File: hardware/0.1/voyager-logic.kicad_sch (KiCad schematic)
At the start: 3 parts, among them J1 USB_C_Receptacle, U1 HD3SS3220, U2 CYUSB3014-BZXx

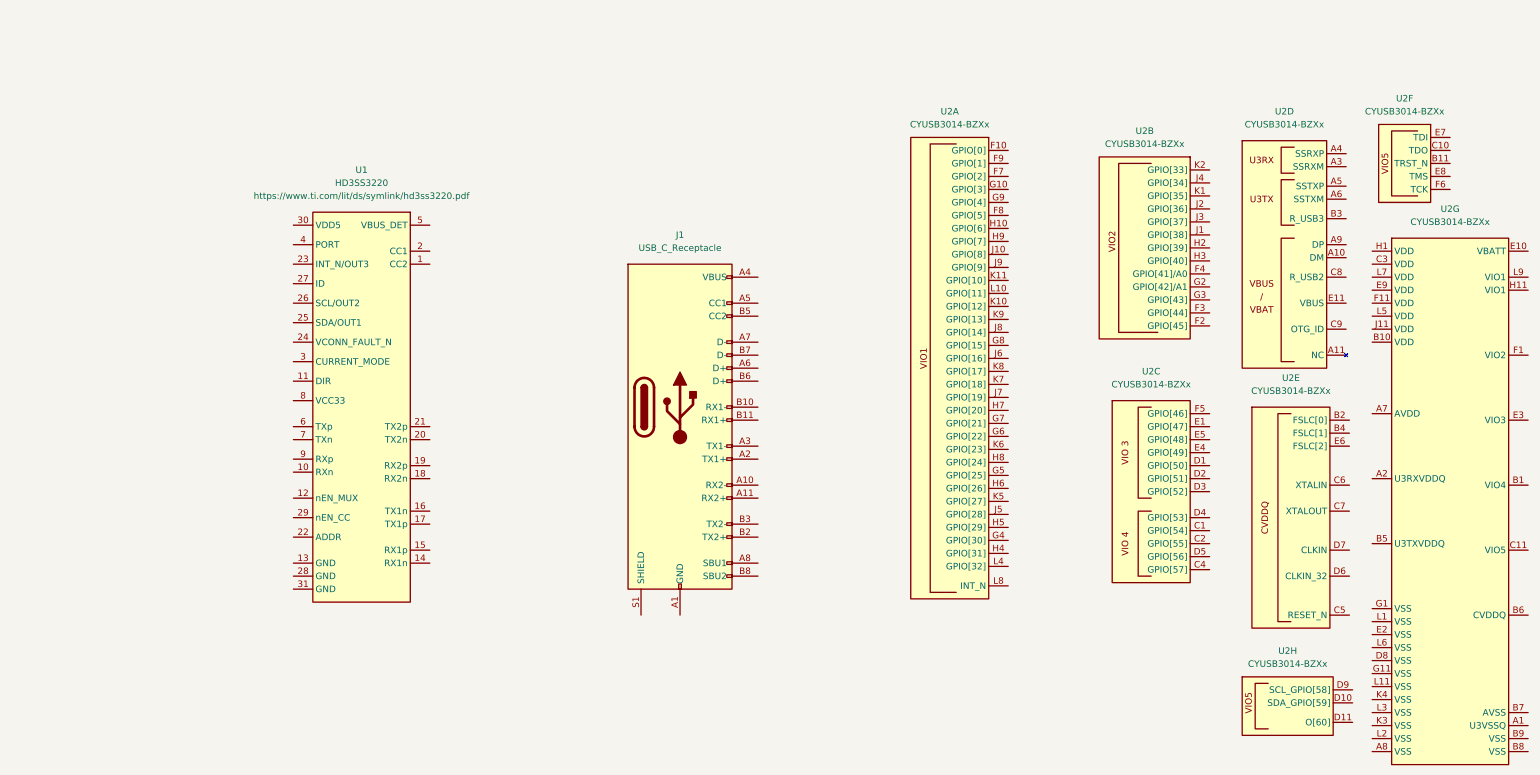
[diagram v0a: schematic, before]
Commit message: wip usb c design
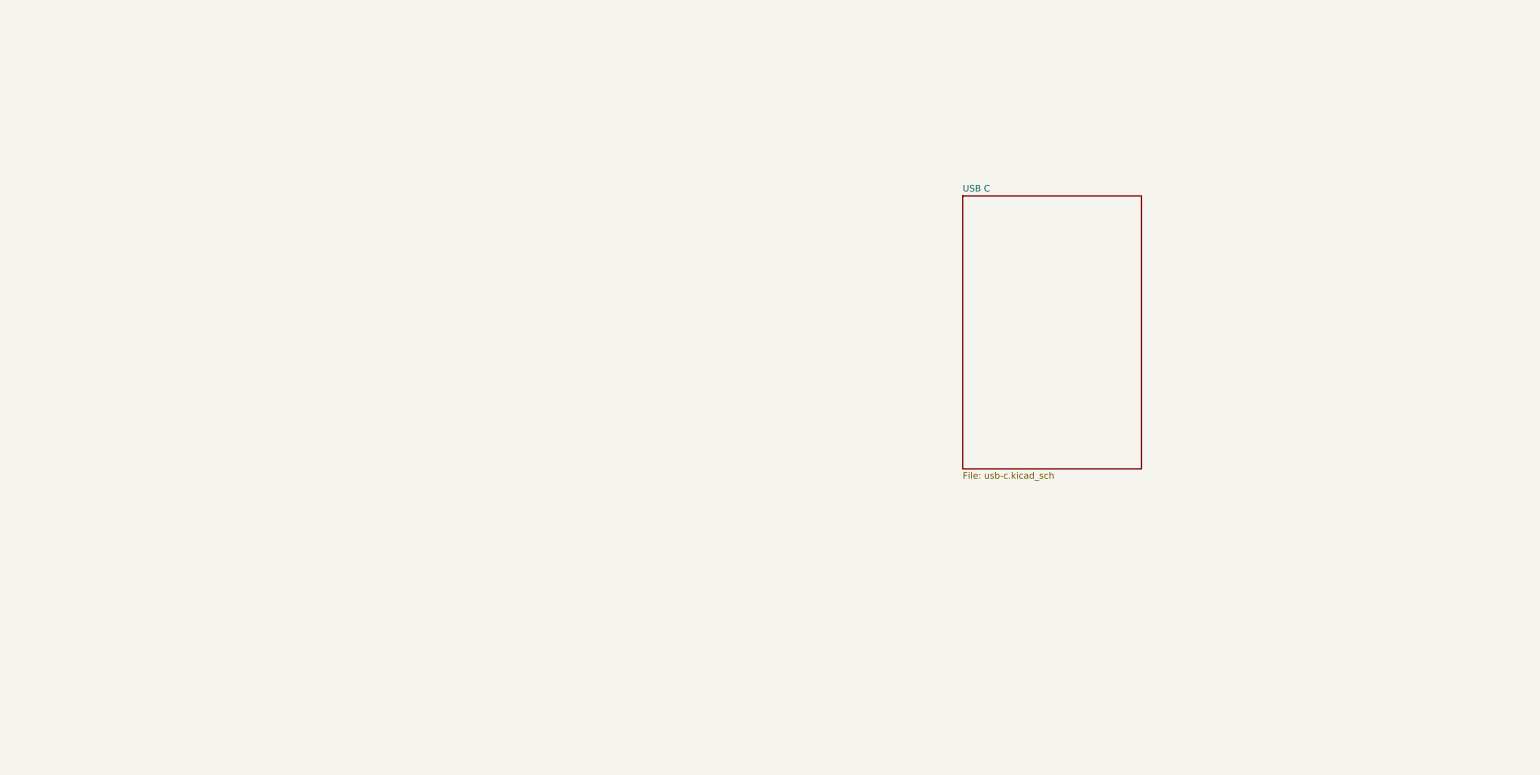
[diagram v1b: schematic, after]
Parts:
- removed J1: USB_C_Receptacle, josh-connectors:USB_C_Receptacle_Amphenol_10137062-00021LF, symbol Connector:USB_C_Receptacle
- removed U1: HD3SS3220, josh-dfn-qfn:Texas_RNH0030A_WQFN-30_2.5x4.5mm_P0.4mm, symbol josh-ic:HD3SS3220
- removed U2: CYUSB3014-BZXx, josh-bga:BGA-121_10x10mm_Layout11x11_P0.8mm, symbol josh-ic:CYUSB3014-BZXx
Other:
- added sheet USB C (usb-c.kicad_sch)

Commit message: continue schematic design
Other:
- sheet USB C renamed USB C Connector
- added sheet Debug (debug.kicad_sch)
- added sheet FX3 USB and Misc (fx3-usb-misc.kicad_sch)
- added sheet Power (power.kicad_sch)
- sheet USB C Connector ports: added USB2_D+, USB2_D-, USB3_RX_N, USB3_RX_P, USB3_TX_N, USB3_TX_P; removed none

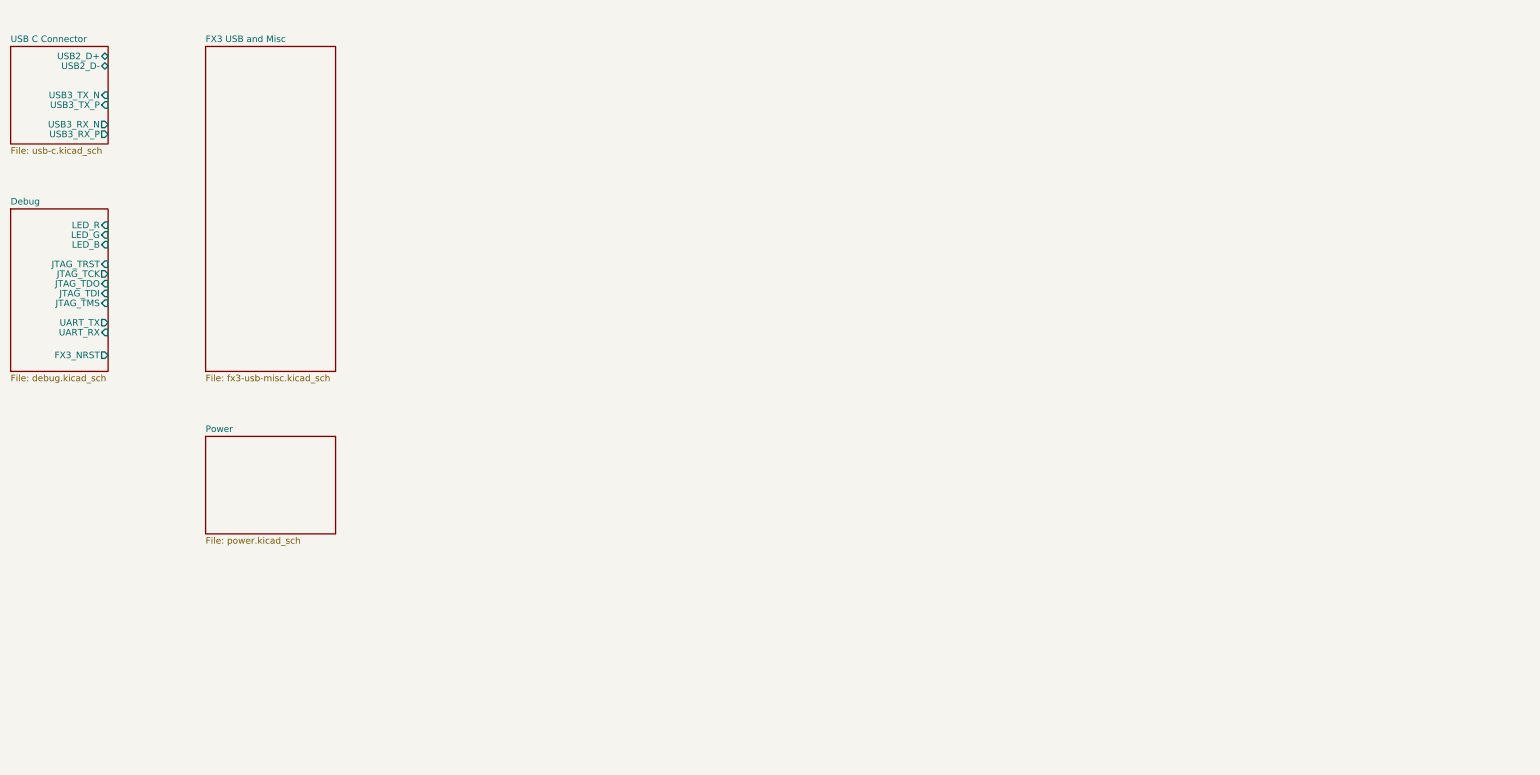
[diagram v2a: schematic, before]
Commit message: first pass schematic done
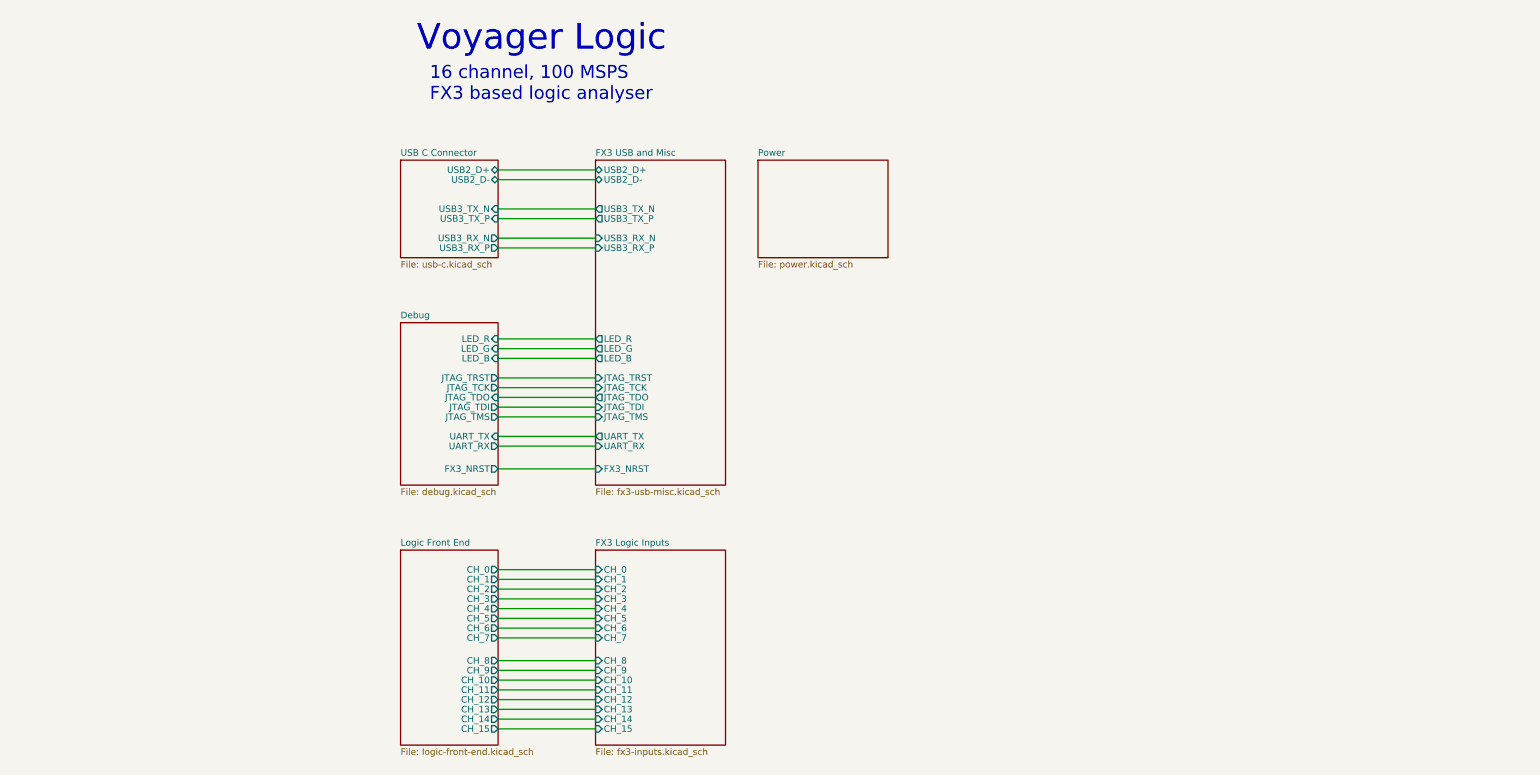
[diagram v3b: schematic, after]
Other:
- added sheet FX3 Logic Inputs (fx3-inputs.kicad_sch)
- added sheet Logic Front End (logic-front-end.kicad_sch)
- sheet FX3 USB and Misc ports: added FX3_NRST, JTAG_TCK, JTAG_TDI, JTAG_TDO, JTAG_TMS, JTAG_TRST, LED_B, LED_G, LED_R, UART_RX, UART_TX, USB2_D+, USB2_D-, USB3_RX_N, USB3_RX_P, USB3_TX_N, USB3_TX_P; removed none
- note added: "16 channel, 100 MSPS FX3 based logic analyser"
- note added: "Voyager Logic"
- company: (none) -> Josh Johnson

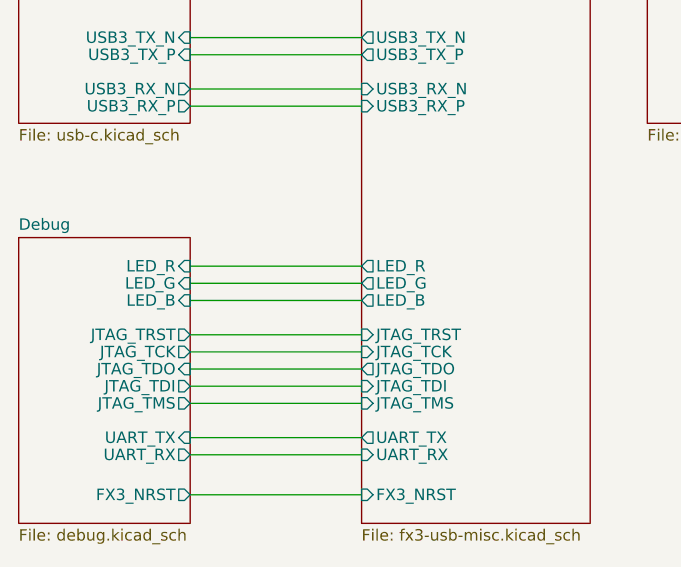
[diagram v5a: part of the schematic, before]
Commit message: break out bga
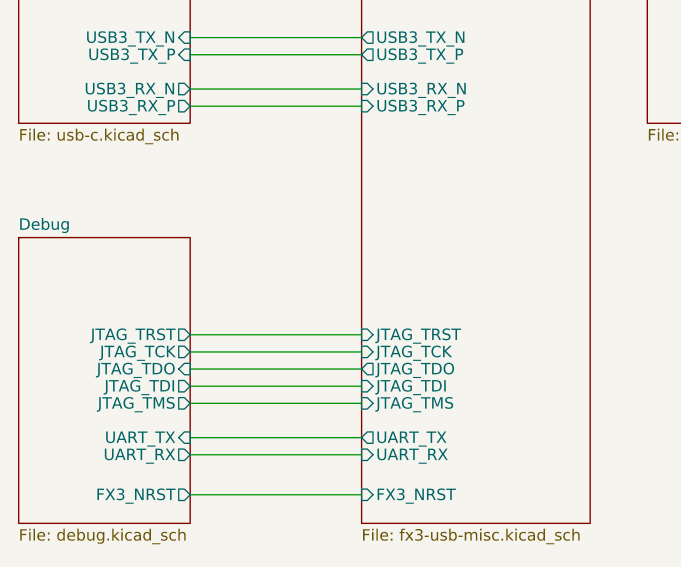
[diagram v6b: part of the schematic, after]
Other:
- sheet Debug ports: added none; removed LED_B, LED_G, LED_R
- sheet FX3 USB and Misc ports: added none; removed LED_B, LED_G, LED_R
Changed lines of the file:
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@@
-    (stroke (width 0) (type default) (color 0 0 0 0))
-  )
-  (wire (pts (xy 120.65 86.36) (xy 139.7 86.36))
-    (stroke (width 0) (type default) (color 0 0 0 0))
-  )
-  (wire (pts (xy 120.65 84.455) (xy 139.7 84.455))
     (stroke (width 0) (type default) (color 0 0 0 0))
   )
@@
   )
   (wire (pts (xy 120.65 129.54) (xy 139.7 129.54))
-    (stroke (width 0) (type default) (color 0 0 0 0))
-  )
-  (wire (pts (xy 120.65 82.55) (xy 139.7 82.55))
     (stroke (width 0) (type default) (color 0 0 0 0))
   )
@@
       (effects (font (size 1.27 1.27)) (justify left))
     )
-    (pin "LED_R" output (at 139.7 82.55 180)
-      (effects (font (size 1.27 1.27)) (justify left))
-    )
-    (pin "LED_G" output (at 139.7 84.455 180)
-      (effects (font (size 1.27 1.27)) (justify left))
-    )
-    (pin "LED_B" output (at 139.7 86.36 180)
-      (effects (font (size 1.27 1.27)) (justify left))
-    )
     (pin "UART_RX" input (at 139.7 103.505 180)
       (effects (font (size 1.27 1.27)) (justify left))
@@
     (property "Sheet file" "debug.kicad_sch" (id 1) (at 101.6 111.7096 0)
       (effects (font (size 1.27 1.27)) (justify left top))
-    )
-    (pin "LED_G" input (at 120.65 84.455 0)
-      (effects (font (size 1.27 1.27)) (justify right))
-    )
-    (pin "LED_R" input (at 120.65 82.55 0)
-      (effects (font (size 1.27 1.27)) (justify right))
-    )
-    (pin "LED_B" input (at 120.65 86.36 0)
-      (effects (font (size 1.27 1.27)) (justify right))
     )
     (pin "JTAG_TDO" input (at 120.65 93.98 0)
@@
       (reference "#PWR0109") (unit 1) (value "+3V3") (footprint "")
     )
+    (path "/34108571-8a13-4907-805c-2f365e2118d7/6cc89465-3d75-4bc8-bb91-d3c503c51d6a"
+      (reference "#PWR0110") (unit 1) (value "GND") (footprint "")
+    )
+    (path "/34108571-8a13-4907-805c-2f365e2118d7/6f61fb2b-6cee-4cc1-8045-1ca27cd354ef"
+      (reference "#PWR0111") (unit 1) (value "GND") (footprint "")
+    )
+    (path "/34108571-8a13-4907-805c-2f365e2118d7/639b0c3d-dac7-4b23-bece-6eccd2ad0769"
+      (reference "#PWR0112") (unit 1) (value "VIO") (footprint "")
+    )
+    (path "/34108571-8a13-4907-805c-2f365e2118d7/c09d40dd-80ed-4709-9c8d-895ad8d55f7e"
+      (reference "#PWR0113") (unit 1) (value "VIO") (footprint "")
+    )
+    (path "/34108571-8a13-4907-805c-2f365e2118d7/e03451ad-d073-4286-a4df-3056f6ccc6ea"
+      (reference "#PWR0114") (unit 1) (value "VIO") (footprint "")
+    )
+    (path "/34108571-8a13-4907-805c-2f365e2118d7/894625ee-ab22-4331-96b7-7b5ed614c6ee"
+      (reference "#PWR0115") (unit 1) (value "GND") (footprint "")
+    )
     (path "/5286cad2-2a6a-4921-931f-2983217525ad/254e0716-875b-410b-a239-ce020285111d"
       (reference "#PWR0201") (unit 1) (value "+5V") (footprint "")
@@
       (reference "#PWR0313") (unit 1) (value "GND") (footprint "")
     )
-    (path "/8ac79583-bc77-4b1e-8425-63e8dca8c0a8/26ac7452-eafd-48e0-aef6-2c18f1e2e69c"
-      (reference "#PWR0314") (unit 1) (value "GND") (footprint "")
-    )
     (path "/95b5a924-9126-4392-8281-2448ce6a0235/54e9048b-e0cc-4929-a6d3-c371e9ec2065"
       (reference "#PWR0401") (unit 1) (value "+3V3") (footprint "")
     )
-    (path "/95b5a924-9126-4392-8281-2448ce6a0235/644005f6-afba-4a5c-a3d7-f012003cf8a5"
-      (reference "#PWR0402") (unit 1) (value "+3V3") (footprint "")
-    )
     (path "/95b5a924-9126-4392-8281-2448ce6a0235/1f4c771c-e8e9-4842-b52e-fa6f7d8d39fe"
       (reference "#PWR0403") (unit 1) (value "GND") (footprint "")
@@
     )
     (path "/5286cad2-2a6a-4921-931f-2983217525ad/0028f935-284b-4032-a9e9-fc6c9a5521e7"
-      (reference "C201") (unit 1) (value "4u7") (footprint "Capacitor_SMD:C_0402_1005Metric")
+      (reference "C201") (unit 1) (value "10u") (footprint "Capacitor_SMD:C_0603_1608Metric")
     )
     (path "/5286cad2-2a6a-4921-931f-2983217525ad/d173c712-b6fa-4f0b-9c30-e2074b7d8580"
@@
     )
     (path "/5286cad2-2a6a-4921-931f-2983217525ad/cb095de1-530b-4c92-836a-e1d8f3413b7f"
-      (reference "C203") (unit 1) (value "470n") (footprint "Capacitor_SMD:C_0402_1005Metric")
+      (reference "C203") (unit 1) (value "100n") (footprint "Capacitor_SMD:C_0201_0603Metric")
     )
     (path "/5286cad2-2a6a-4921-931f-2983217525ad/f0359792-ecb0-44f6-93bc-ce78418d6903"
@@
     )
     (path "/5286cad2-2a6a-4921-931f-2983217525ad/2289b62d-762e-4bd3-b07d-395fa288f406"
-      (reference "C205") (unit 1) (value "470n") (footprint "Capacitor_SMD:C_0402_1005Metric")
+      (reference "C205") (unit 1) (value "100n") (footprint "Capacitor_SMD:C_0201_0603Metric")
     )
     (path "/5286cad2-2a6a-4921-931f-2983217525ad/c96c4065-a3db-4b4a-8c1f-2961f21fbe33"
-      (reference "C206") (unit 1) (value "470n") (footprint "Capacitor_SMD:C_0402_1005Metric")
+      (reference "C206") (unit 1) (value "100n") (footprint "Capacitor_SMD:C_0201_0603Metric")
     )
     (path "/5286cad2-2a6a-4921-931f-2983217525ad/580c0b5a-f825-4eca-a55d-85effc48e19f"
-      (reference "C207") (unit 1) (value "470n") (footprint "Capacitor_SMD:C_0402_1005Metric")
+      (reference "C207") (unit 1) (value "100n") (footprint "Capacitor_SMD:C_0201_0603Metric")
     )
     (path "/5286cad2-2a6a-4921-931f-2983217525ad/5ec7a8e3-575f-425d-9246-1b351c6c30b3"
       (reference "C208") (unit 1) (value "100n") (footprint "Capacitor_SMD:C_0402_1005Metric")
     )
-    (path "/8ac79583-bc77-4b1e-8425-63e8dca8c0a8/1403dd68-e986-4c28-b63c-b3e7a91d6fb6"
-      (reference "C301") (unit 1) (value "100n") (footprint "Capacitor_SMD:C_0402_1005Metric")
-    )
-    (path "/8ac79583-bc77-4b1e-8425-63e8dca8c0a8/1d4cb2c3-7269-4135-bd32-a26a18c7eba8"
-      (reference "C302") (unit 1) (value "100n") (footprint "Capacitor_SMD:C_0402_1005Metric")
-    )
     (path "/8ac79583-bc77-4b1e-8425-63e8dca8c0a8/7bb01e67-276e-403b-8eed-4e05264e6203"
       (reference "C303") (unit 1) (value "13p") (footprint "Capacitor_SMD:C_0402_1005Metric")
@@
       (reference "D201") (unit 1) (value "SMF9.0CA") (footprint "josh-passives-smt:D_SOD-123FL")
     )
-    (path "/95b5a924-9126-4392-8281-2448ce6a0235/ee25d5ed-34d6-4108-9012-4eaaf5ea9462"
-      (reference "D401") (unit 1) (value "LED_RGBA") (footprint "josh-led:LED_TRI_2020")
-    )
     (path "/95b5a924-9126-4392-8281-2448ce6a0235/0da573dd-1ecb-47d7-a1d2-6a70ea264ca9"
       (reference "D402") (unit 1) (value "LED_RGBA") (footprint "josh-led:LED_TRI_2020")
@@
     )
     (path "/5286cad2-2a6a-4921-931f-2983217525ad/c47f9a2e-4601-4de5-af31-5e0f9978a409"
-      (reference "F201") (unit 1) (value "500mA") (footprint "josh-passives-smt:Fuse_0603_1608Metric")
+      (reference "F201") (unit 1) (value "500mA") (footprint "josh-passives-smt:Fuse_0805_2012Metric")
     )
     (path "/5286cad2-2a6a-4921-931f-2983217525ad/62d0a369-d24e-44cf-8ca7-58bea87cac3e"
@@
       (reference "R207") (unit 1) (value "0R") (footprint "Resistor_SMD:R_0402_1005Metric")
     )
-    (path "/8ac79583-bc77-4b1e-8425-63e8dca8c0a8/a0615155-7b33-4b1f-8f41-3b7d7735d745"
-      (reference "R301") (unit 1) (value "10K") (footprint "Resistor_SMD:R_0402_1005Metric")
-    )
     (path "/8ac79583-bc77-4b1e-8425-63e8dca8c0a8/ce0be23c-c221-47a8-9987-cf95e4bf4bc5"
       (reference "R302") (unit 1) (value "200R") (footprint "Resistor_SMD:R_0402_1005Metric")
@@
       (reference "R307") (unit 1) (value "DNP") (footprint "Resistor_SMD:R_0402_1005Metric")
     )
-    (path "/8ac79583-bc77-4b1e-8425-63e8dca8c0a8/f50aa7a8-2121-4ba8-aae5-ee51280479b0"
-      (reference "R308") (unit 1) (value "10K") (footprint "Resistor_SMD:R_0402_1005Metric")
-    )
-    (path "/95b5a924-9126-4392-8281-2448ce6a0235/b1014a74-1d4b-47fa-b4ab-ce729eaa7518"
-      (reference "R401") (unit 1) (value "1K") (footprint "Resistor_SMD:R_0402_1005Metric")
-    )
     (path "/95b5a924-9126-4392-8281-2448ce6a0235/732e1820-4199-4046-98df-b2f84b87a832"
       (reference "R402") (unit 1) (value "10K") (footprint "Resistor_SMD:R_0402_1005Metric")
     )
-    (path "/95b5a924-9126-4392-8281-2448ce6a0235/6cc2bc11-407a-403e-a9c0-864203c24e4f"
-      (reference "R403") (unit 1) (value "1K") (footprint "Resistor_SMD:R_0402_1005Metric")
-    )
-    (path "/95b5a924-9126-4392-8281-2448ce6a0235/5b599427-92c8-4d0a-8539-b45d85dbda0f"
-      (reference "R404") (unit 1) (value "1K") (footprint "Resistor_SMD:R_0402_1005Metric")
-    )
     (path "/95b5a924-9126-4392-8281-2448ce6a0235/34c540d4-6779-4037-a36a-6ea8a08593da"
       (reference "R405") (unit 1) (value "1K") (footprint "Resistor_SMD:R_0402_1005Metric")
@@
       (reference "R520") (unit 1) (value "909K") (footprint "Resistor_SMD:R_0402_1005Metric")
     )
+    (path "/34108571-8a13-4907-805c-2f365e2118d7/590d2f80-3bbe-4afd-a38c-49e2b5547e38"
+      (reference "R601") (unit 1) (value "DNP") (footprint "Resistor_SMD:R_0402_1005Metric")
+    )
+    (path "/34108571-8a13-4907-805c-2f365e2118d7/fbe58de2-6492-4775-83e5-0e4ff73720f7"
+      (reference "R602") (unit 1) (value "10K") (footprint "Resistor_SMD:R_0402_1005Metric")
+    )
+    (path "/34108571-8a13-4907-805c-2f365e2118d7/bc0759c4-2747-47bc-9694-e0e19d29204d"
+      (reference "R603") (unit 1) (value "10K") (footprint "Resistor_SMD:R_0402_1005Metric")
+    )
+    (path "/34108571-8a13-4907-805c-2f365e2118d7/64456d0b-1501-4259-afe2-3d63e9438a12"
+      (reference "R604") (unit 1) (value "DNP") (footprint "Resistor_SMD:R_0402_1005Metric")
+    )
+    (path "/34108571-8a13-4907-805c-2f365e2118d7/1df94546-64ae-4039-8855-2afc408c5202"
+      (reference "R605") (unit 1) (value "DNP") (footprint "Resistor_SMD:R_0402_1005Metric")
+    )
+    (path "/34108571-8a13-4907-805c-2f365e2118d7/d3b62284-d74b-42b2-8939-6bdba3696596"
+      (reference "R606") (unit 1) (value "DNP") (footprint "Resistor_SMD:R_0402_1005Metric")
+    )
     (path "/1766326e-181a-491d-a0e4-e97d1588585c/136dbe3e-fa3d-4a01-8412-24c10d69ed17"
